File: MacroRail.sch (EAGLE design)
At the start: 21 parts, among them CN2 1X4-3.5MM, CN3 SJ1-2503A, Q1 TIP120, U1 ESP32DEVKITC, U2 TMC2209-V1.2+INDEX

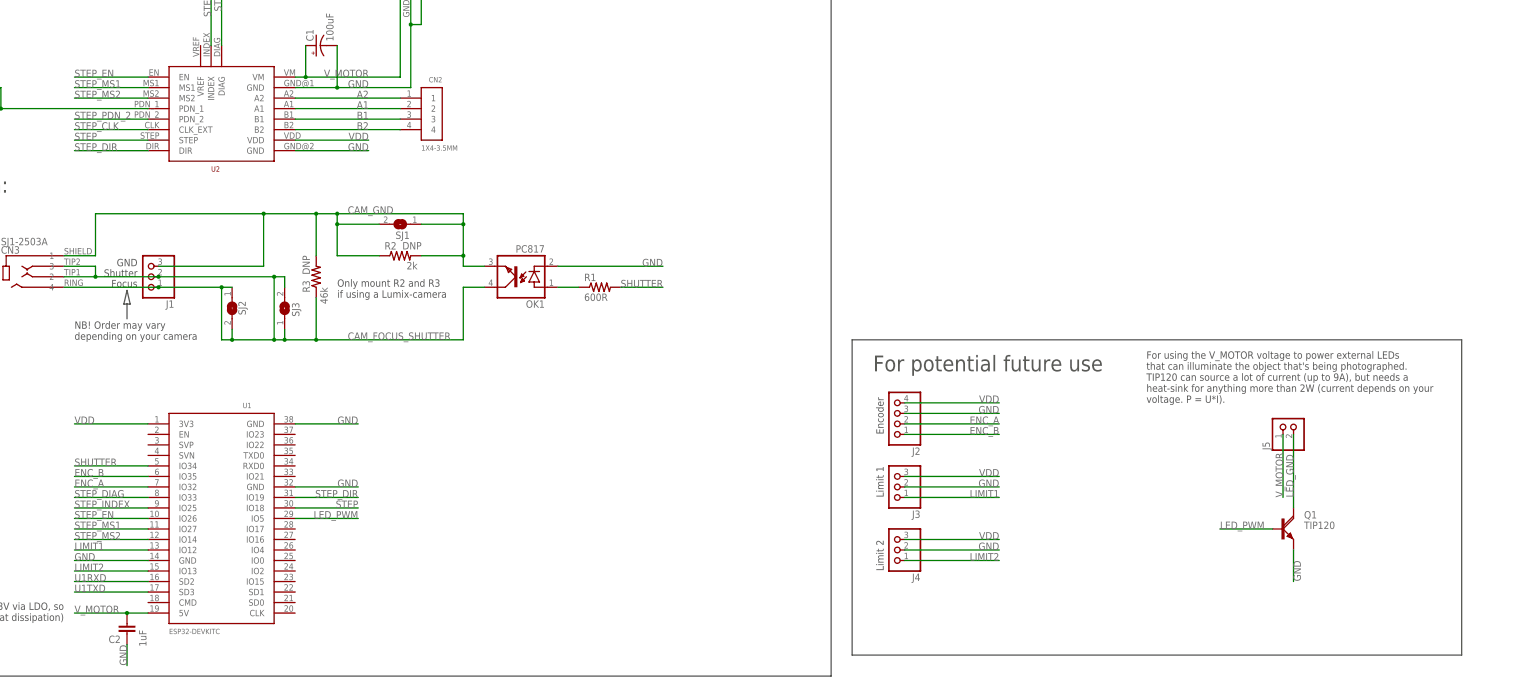
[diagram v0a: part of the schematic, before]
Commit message: V1 Revision 1
Large redesign of the board. Made board wider (50x80mm now). Moved connections to make them more accessible when PCB is mounted on macro slider. Added transistor for driving LED illumination. Added more connections to TMC driver (UART and Index). Added capacitance to EN pin after noticing this helps with automatic bootloader entry during programming.
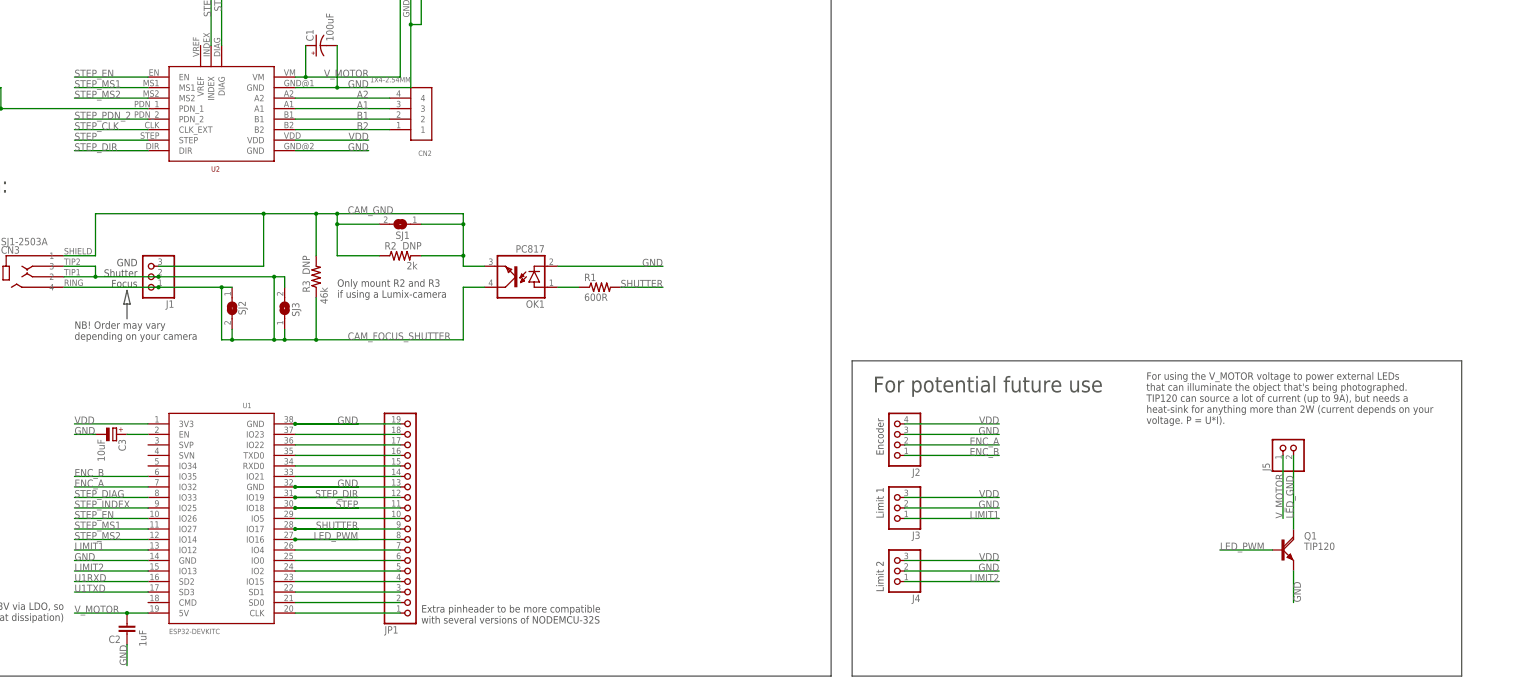
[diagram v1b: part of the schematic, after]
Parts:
- added C3: 10uF, rcl:CPOL-EUE1.8-4
- added JP1: (no value), pinhead-custom:PINHD-1X19
- CN1: device adafruit:DCBARRELPTH -> 00-Random-Components-Simen:DCBARRELPTH
- CN2: value 1X4-3.5MM -> 1X4-2.54MM; device adafruit:1X4-3.5MM -> 00-Random-Components-Simen:1X4-2.54MM
- OK1: device optocoupler:PC817 -> 00-Random-Components-Simen:PC817
- U1: value ESP32DEVKITC -> ESP32DEVKITCWIDE; device ESP32-DEVKITC:ESP32DEVKITC -> ESP32-DEVKITC:ESP32DEVKITCWIDE
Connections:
- new net N$10: JP1.6, U1.IO0
- new net N$11: JP1.5, U1.IO2
- new net N$12: JP1.4, U1.IO15
- new net N$13: JP1.3, U1.SD1
- new net N$14: JP1.2, U1.SD0
- new net N$15: JP1.1, U1.CLK
- new net N$2: C3.+, U1.EN
- new net N$3: JP1.18, U1.IO23
- new net N$4: JP1.17, U1.IO22
- new net N$5: JP1.16, U1.TXD0
- new net N$6: JP1.15, U1.RXD0
- new net N$7: JP1.14, U1.IO21
- new net N$8: JP1.10, U1.IO5
- new net N$9: JP1.7, U1.IO4
- net A1: now also CN2.3; no longer CN2.2
- net A2: now also CN2.4; no longer CN2.1
- net B1: now also CN2.2; no longer CN2.3
- net B2: now also CN2.1; no longer CN2.4
- net GND: now also C3.-, JP1.13, JP1.19
- net LED_PWM: now also JP1.8, U1.IO16; no longer U1.IO5
- net SHUTTER: now also JP1.9, U1.IO17; no longer U1.IO34
- net STEP: now also JP1.11
- net STEP_DIR: now also JP1.12
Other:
- note added: "Extra pinheader to be more compatible with several versions of NODEMCU-32S"
- moved on the sheet: CN2, J2, J3, J4, J5, Q1

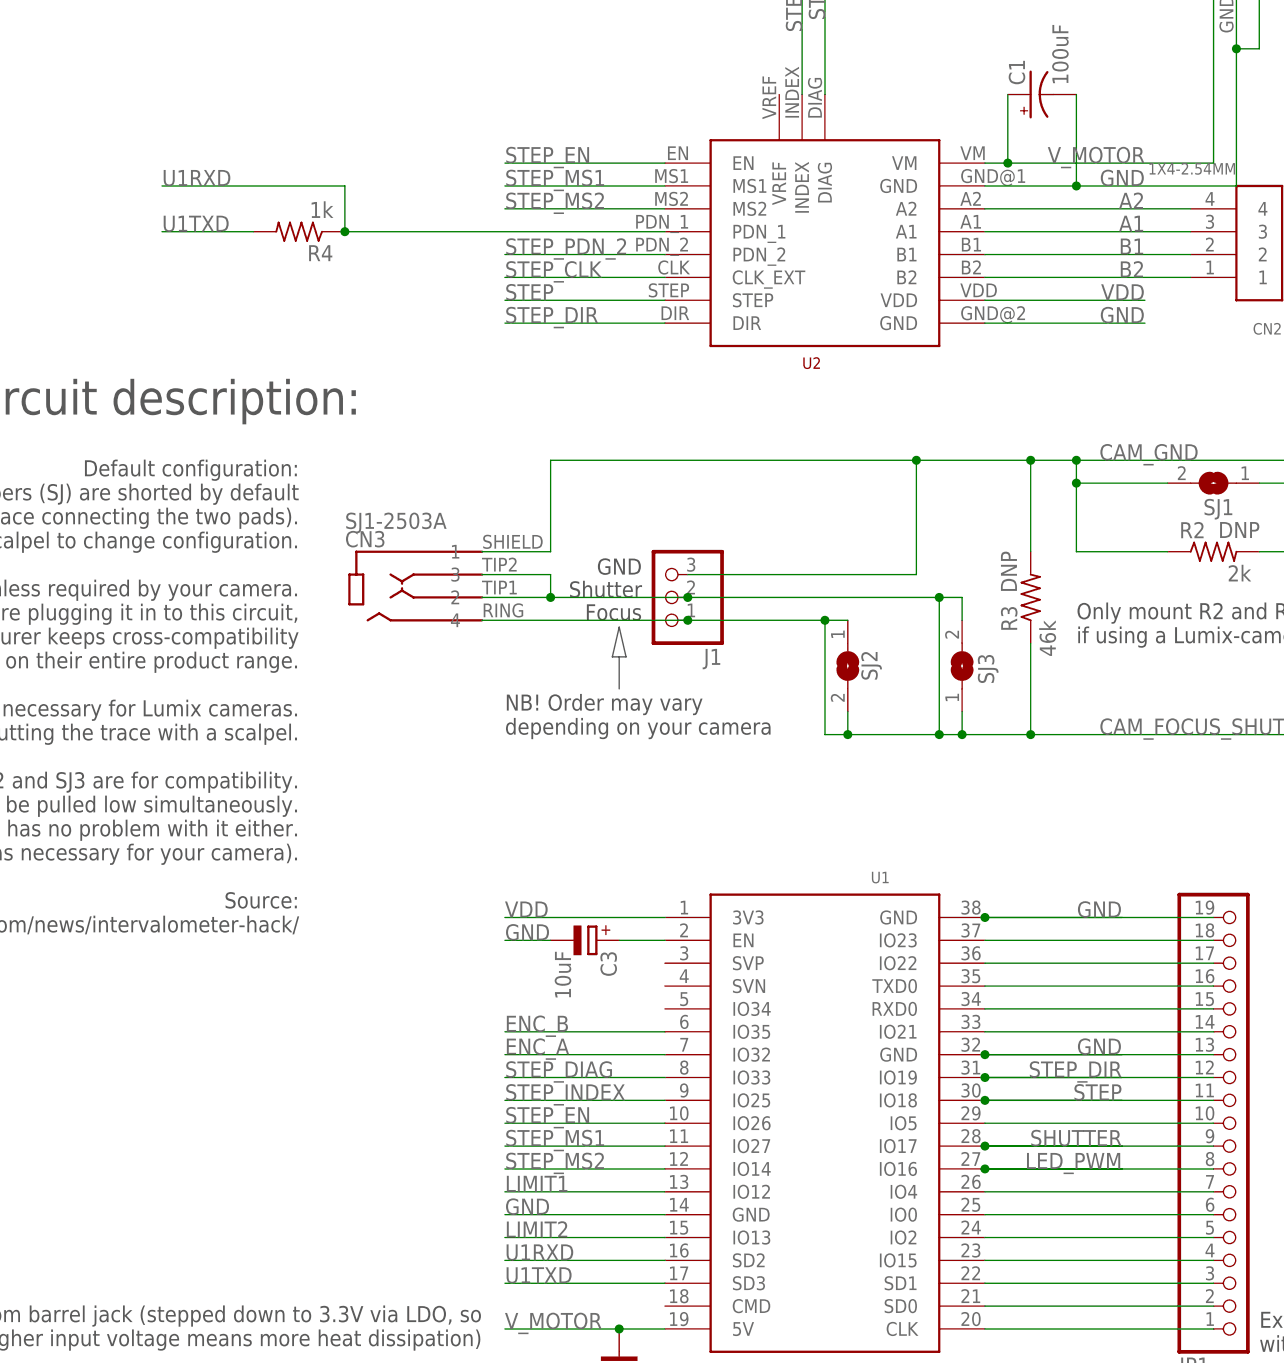
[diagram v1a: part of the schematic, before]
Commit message: Move TMC UART communication to Serial2
Serial1 is already occupied by the ESP flash, so we need to use Serial2 instead. This interface was already in use by the SHUTTER- and LED_PWM-signals, so they had to be moved as well.
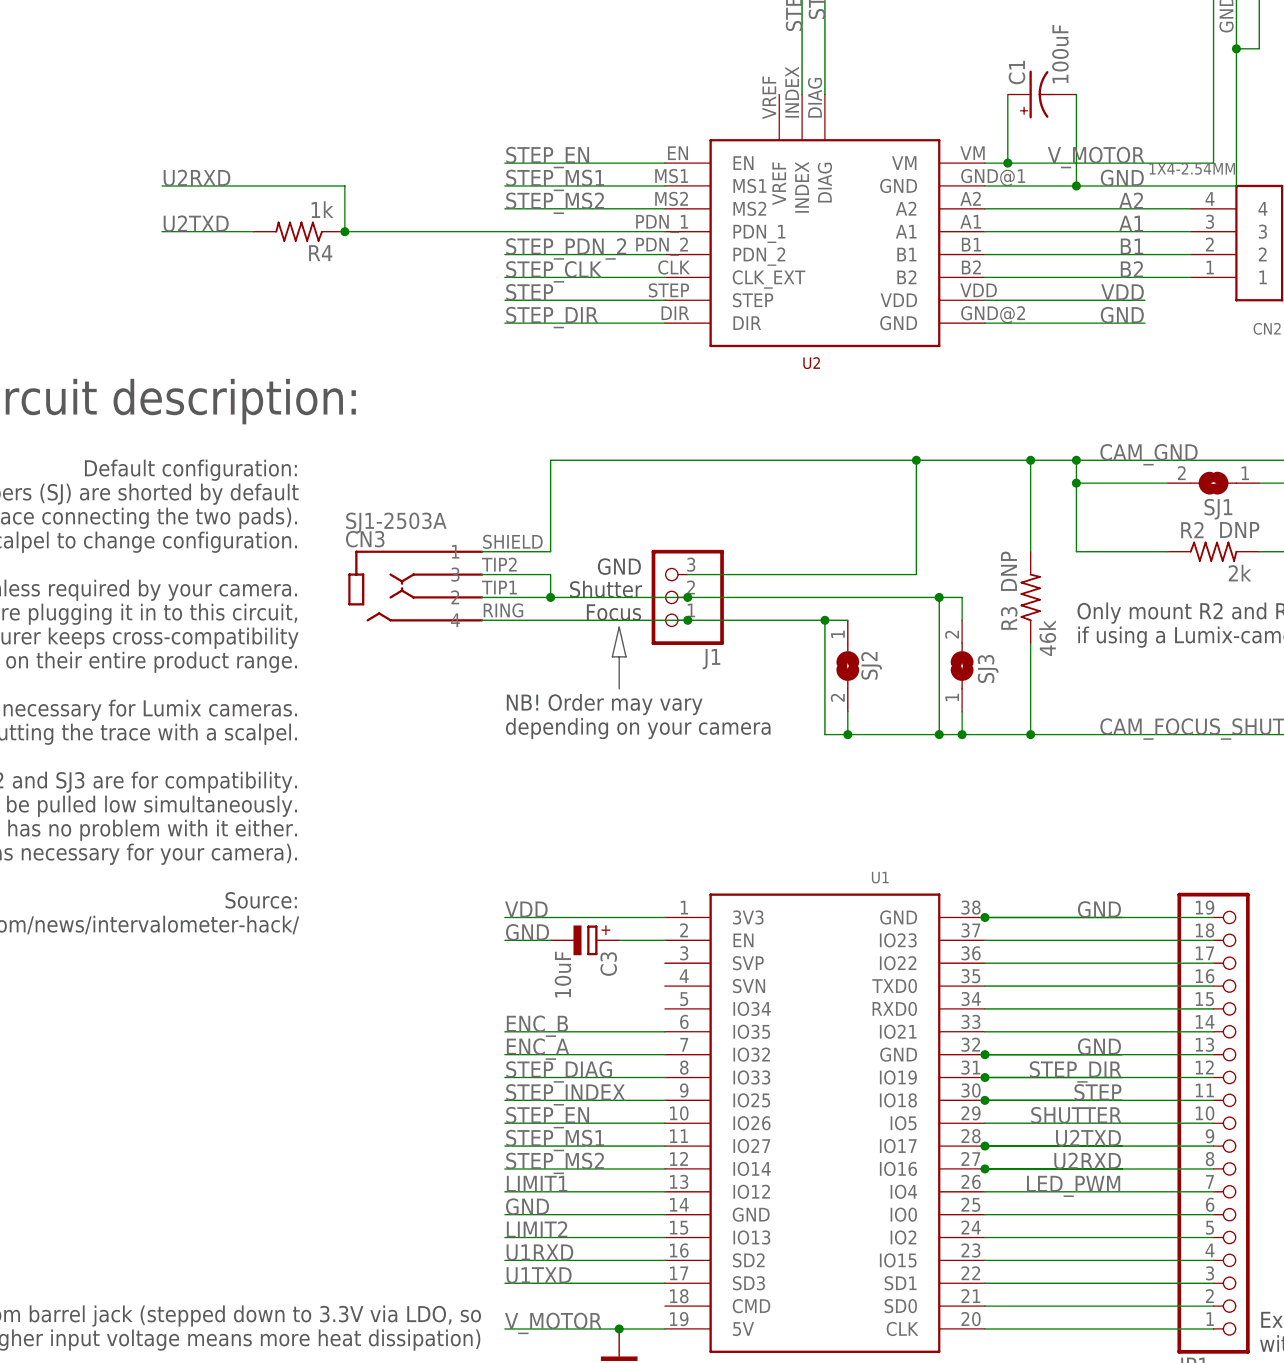
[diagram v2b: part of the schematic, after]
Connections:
- removed net N$8: JP1.10, U1.IO5
- removed net N$9: JP1.7, U1.IO4
- new net U2RXD: JP1.8, R4.1, U1.IO16, U2.PDN_1
- new net U2TXD: JP1.9, R4.2, U1.IO17
- net LED_PWM: now also JP1.7, U1.IO4; no longer JP1.8, U1.IO16
- net SHUTTER: now also JP1.10, U1.IO5; no longer JP1.9, U1.IO17
- net U1RXD: no longer R4.1, U2.PDN_1
- net U1TXD: no longer R4.2
